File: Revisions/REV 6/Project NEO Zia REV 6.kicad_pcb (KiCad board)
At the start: 2 copper layers, 220.2 x 220.2 mm, 142 parts, among them J1 TSM-103-02-L-SH-LC, J2 TSM-103-02-L-SH-LC

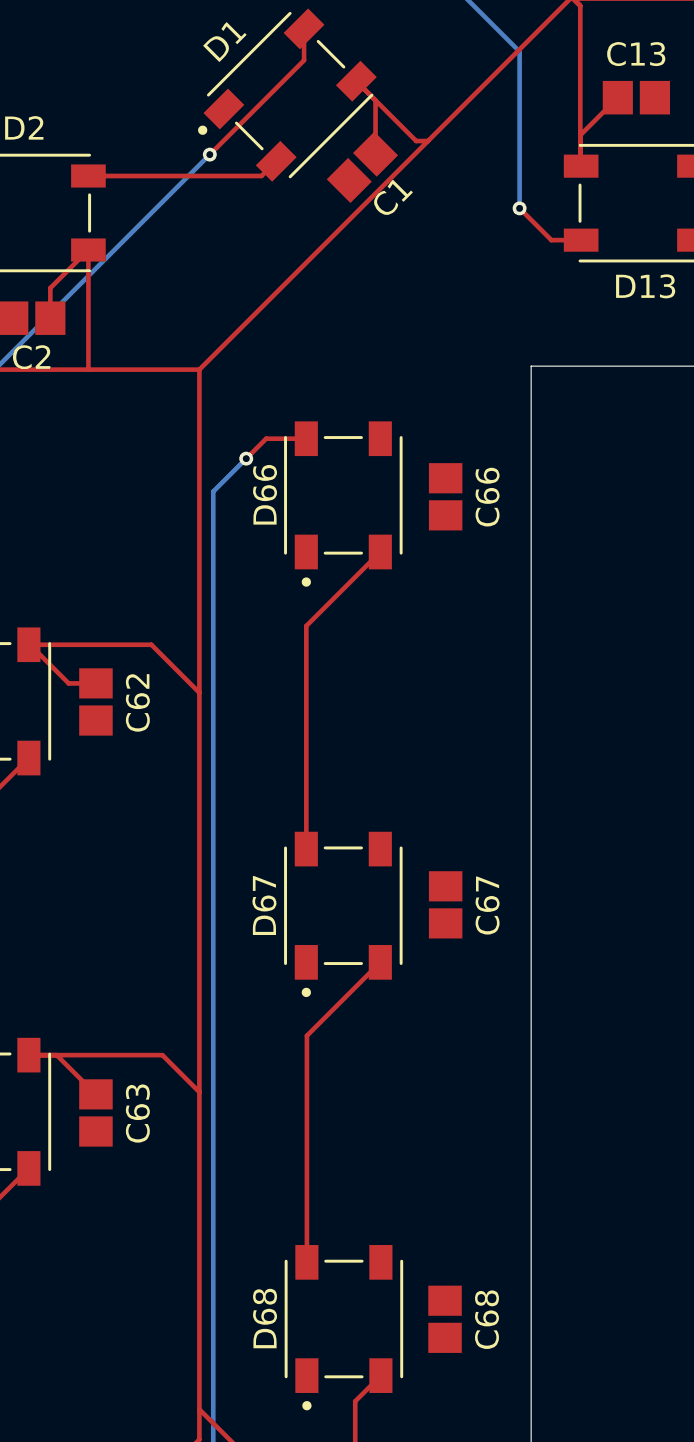
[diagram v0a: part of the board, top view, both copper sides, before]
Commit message: - Added "For more info visit: https://github.com/JZRod/Project-NEO-Zia" to all versions 	# backported to all pre-existing versions - Fixed voltage regulator tab being shorted to GND 	# Backported to all relevant rev's - Added gbr, step, and csv files to all versions (except original) - Fixed sheet information to match REVISION NOTES.txt
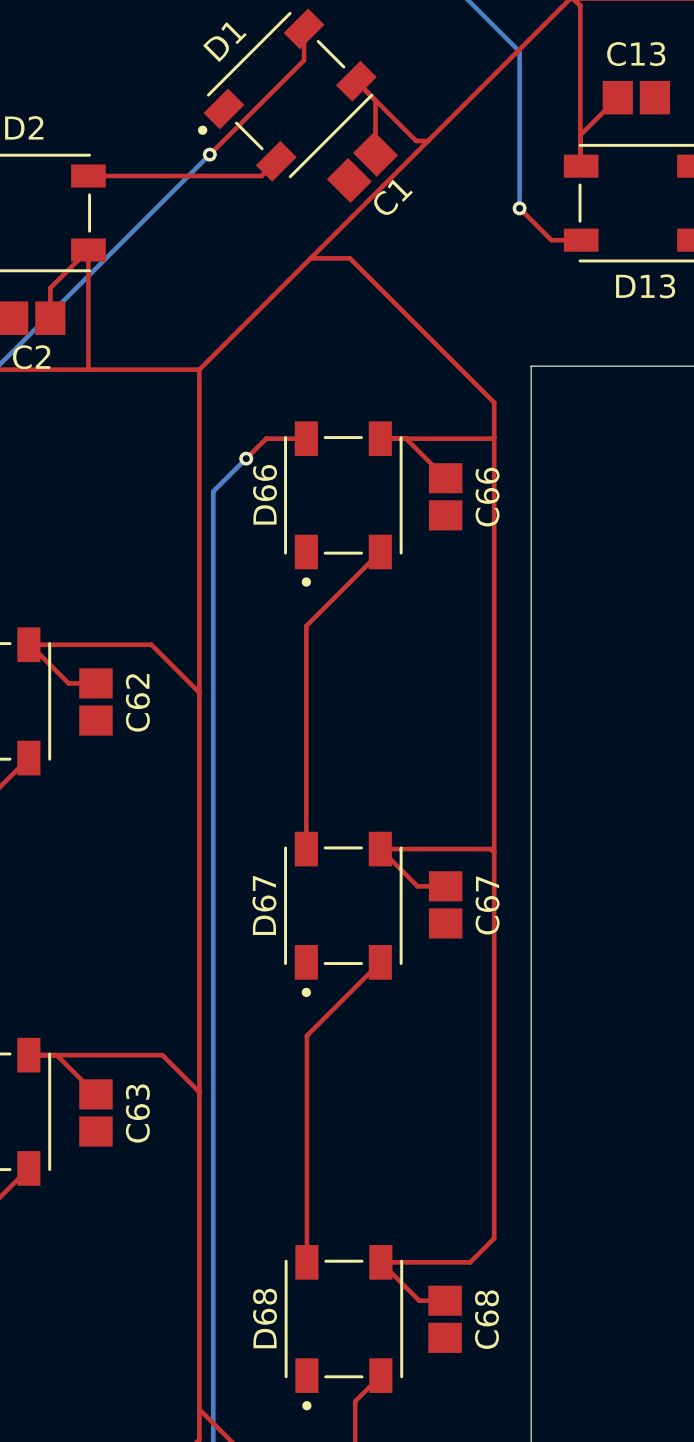
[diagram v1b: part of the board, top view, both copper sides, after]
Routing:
- net +5V: track 1618.4 -> 1690.8 mm
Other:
- board text added: "For more info visit: https://github.com/JZRod/Project-NEO-Zia"
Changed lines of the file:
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@@
 	(paper "A3")
 	(title_block
-		(date "2025-10-25")
+		(title "Project NEO Zia")
+		(date "9/10/2025")
+		(rev "6")
+		(comment 1 "Started work on 6/17/2025")
 	)
 	(layers
@@
 		(layer "Edge.Cuts")
 	)
+	(gr_text "For more info visit: https://github.com/JZRod/Project-NEO-Zia"
+		(at 283.175 193.6 0)
+		(layer "B.SilkS")
+		(effects
+			(font
+				(size 1.5 1.5)
+				(thickness 0.3)
+				(bold yes)
+			)
+			(justify left bottom mirror)
+		)
+	)
 	(segment
 		(start 209.925 188.25)
@@
 	)
 	(segment
+		(start 227.475 198.05)
+		(end 227.475 199.55)
+		(width 0.2)
+		(layer "F.Cu")
+		(net 4)
+	)
+	(segment
 		(start 277.172201 155.765299)
 		(end 275.55 157.3875)
@@
 	)
 	(segment
+		(start 219.5375 191.8125)
+		(end 221.2375 191.8125)
+		(width 0.2)
+		(layer "F.Cu")
+		(net 4)
+	)
+	(segment
 		(start 156.477799 178.55)
 		(end 156.477799 177.322201)
@@
 	)
 	(segment
+		(start 221.2375 191.8125)
+		(end 227.475 198.05)
+		(width 0.2)
+		(layer "F.Cu")
+		(net 4)
+	)
+	(segment
 		(start 177.457335 148.972158)
 		(end 178.361218 149.876041)
@@
 	)
 	(segment
+		(start 227.475 217.5)
+		(end 227.475 234.2)
+		(width 0.2)
+		(layer "F.Cu")
+		(net 4)
+	)
+	(segment
 		(start 183.025 235.15)
 		(end 184.5 233.675)
@@
 	)
 	(segment
+		(start 225.35 236.897201)
+		(end 224.234701 236.897201)
+		(width 0.2)
+		(layer "F.Cu")
+		(net 4)
+	)
+	(segment
 		(start 106.075 175.675)
 		(end 105 175.675)
@@
 	)
 	(segment
+		(start 227.4125 199.6125)
+		(end 227.475 199.55)
+		(width 0.2)
+		(layer "F.Cu")
+		(net 4)
+	)
+	(segment
 		(start 224.102323 186.7375)
 		(end 224.6125 186.7375)
@@
 	)
 	(segment
+		(start 224.234701 236.897201)
+		(end 222.575 235.2375)
+		(width 0.2)
+		(layer "F.Cu")
+		(net 4)
+	)
+	(segment
 		(start 178.6 195.375)
 		(end 166.35 195.375)
@@
 	)
 	(segment
+		(start 224.159701 218.972201)
+		(end 222.55 217.3625)
+		(width 0.2)
+		(layer "F.Cu")
+		(net 4)
+	)
+	(segment
 		(start 158.1 160.45)
 		(end 158.1 166.1)
@@
 	)
 	(segment
+		(start 227.475 199.55)
+		(end 227.475 217.5)
+		(width 0.2)
+		(layer "F.Cu")
+		(net 4)
+	)
+	(segment
 		(start 230.775 152.675)
 		(end 231.725 151.725)
@@
 	)
 	(segment
+		(start 222.55 199.6125)
+		(end 223.665299 199.6125)
+		(width 0.2)
+		(layer "F.Cu")
+		(net 4)
+	)
+	(segment
 		(start 221.25 133.425)
 		(end 215.975 133.425)
@@
 	)
 	(segment
+		(start 227.475 234.2)
+		(end 226.4375 235.2375)
+		(width 0.2)
+		(layer "F.Cu")
+		(net 4)
+	)
+	(segment
 		(start 170.55 167.675)
 		(end 170.55 176.45)
@@
 	)
 	(segment
+		(start 219.5375 191.8125)
+		(end 224.6125 186.7375)
+		(width 0.2)
+		(layer "F.Cu")
+		(net 4)
+	)
+	(segment
 		(start 174.925 176.4875)
 		(end 170.5875 176.4875)
@@
 	)
 	(segment
+		(start 222.55 199.6125)
+		(end 227.4125 199.6125)
+		(width 0.2)
+		(layer "F.Cu")
+		(net 4)
+	)
+	(segment
 		(start 252.447201 139.2625)
 		(end 252.447201 140.477799)
@@
 	)
 	(segment
+		(start 227.3375 217.3625)
+		(end 227.475 217.5)
+		(width 0.2)
+		(layer "F.Cu")
+		(net 4)
+	)
+	(segment
 		(start 156.502799 163.45)
 		(end 156.502799 162.047201)
@@
 	(segment
 		(start 214.725 196.625)
-		(end 224.6125 186.7375)
+		(end 219.5375 191.8125)
 		(width 0.2)
 		(layer "F.Cu")
@@
 	)
 	(segment
+		(start 225.375 218.972201)
+		(end 224.159701 218.972201)
+		(width 0.2)
+		(layer "F.Cu")
+		(net 4)
+	)
+	(segment
 		(start 198.525 78.925)
 		(end 206.1 71.35)
@@
 	)
 	(segment
+		(start 222.55 217.3625)
+		(end 227.3375 217.3625)
+		(width 0.2)
+		(layer "F.Cu")
+		(net 4)
+	)
+	(segment
 		(start 124.1 182.575)
 		(end 112.975 182.575)
@@
 	)
 	(segment
+		(start 223.665299 199.6125)
+		(end 225.375 201.322201)
+		(width 0.2)
+		(layer "F.Cu")
+		(net 4)
+	)
+	(segment
 		(start 141.95 167.675)
 		(end 124.35 167.675)
@@
 		(width 0.2)
 		(layer "F.Cu")
+		(net 4)
+	)
+	(segment
+		(start 226.4375 235.2375)
+		(end 222.575 235.2375)
+		(width 0.2)
+		(layer "F.Cu")
